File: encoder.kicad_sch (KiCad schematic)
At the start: 5 parts, among them IC1 AS5600-ASOT, J1 BM04B-SURS-TFLFSN, SW1 A6S-2104-H

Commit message: Reworked lots
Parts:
- removed SW1: A6S-2104-H, 2_POS_DIP:A6S-2104-H, symbol 2_POS_DIP:A6S-2104-H
- added H1, H2, H3: MountingHole, MountingHole:MountingHole_2.7mm_M2.5_ISO7380, symbol Mechanical:MountingHole
- added R1, R2: R, Resistor_SMD:R_0603_1608Metric_Pad0.98x0.95mm_HandSolder, symbol Device:R
- renumbered IC1 to U1
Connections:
- net +3.3V: now also R1.2
- net DIR: now also R1.1, R2.1
- net GND: now also J1.4 (SDA), R2.2; no longer J1.2 (GND)
- net SDA: now reaches U1.6 (SDA)
- net SDA: now also J1.2 (GND); no longer J1.4 (SDA)
- net SCL: now reaches J1.3 (SCL), U1.7 (SCL)
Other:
- moved on the sheet: J1

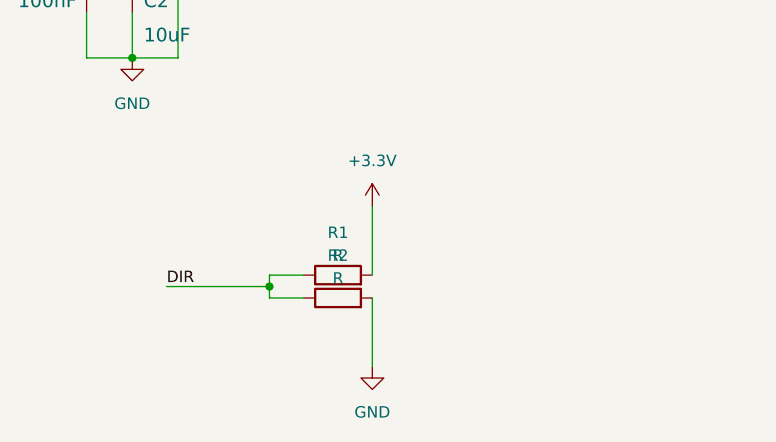
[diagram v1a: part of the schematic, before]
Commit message: schematic tweak
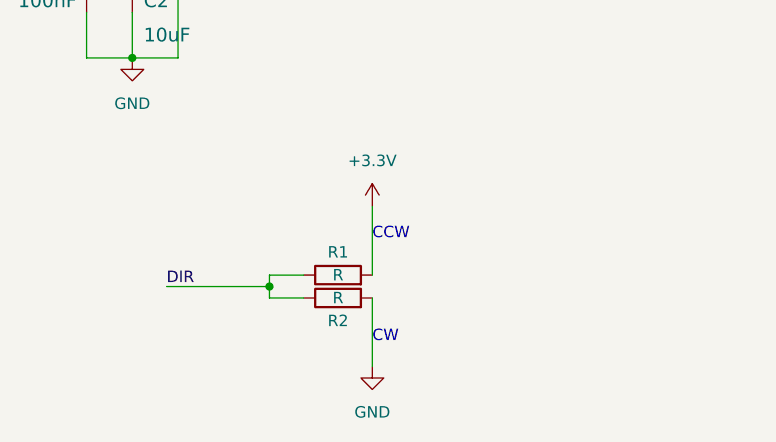
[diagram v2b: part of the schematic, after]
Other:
- note added: "CCW"
- note added: "CW"
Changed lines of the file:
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@@
     (stroke (width 0) (type default) (color 0 0 0 0))
+  )
+  (text "CW" (at 73.66 109.22 0)
+    (effects (font (size 1.27 1.27)) (justify left bottom))
+  )
+  (text "CCW" (at 73.66 97.79 0)
+    (effects (font (size 1.27 1.27)) (justify left bottom))
   )
   (label "SDA" (at 82.55 63.5 0)
@@
   )
   (symbol (lib_id "Device:R") (at 69.85 101.6 90) (unit 1)
-    (in_bom yes) (on_board yes) (fields_autoplaced)
-    (property "Reference" "R1" (id 0) (at 69.85 96.8842 90))
-    (property "Value" "R" (id 1) (at 69.85 99.4211 90))
+    (in_bom yes) (on_board yes)
+    (property "Reference" "R1" (id 0) (at 69.85 99.06 90))
+    (property "Value" "R" (id 1) (at 69.85 101.6 90))
     (property "Footprint" "Resistor_SMD:R_0603_1608Metric_Pad0.98x0.95mm_HandSolder" (id 2) (at 69.85 103.378 90)
       (effects (font (size 1.27 1.27)) hide)
@@
   )
   (symbol (lib_id "Device:R") (at 69.85 104.14 90) (unit 1)
-    (in_bom yes) (on_board yes) (fields_autoplaced)
-    (property "Reference" "R2" (id 0) (at 69.85 99.4242 90))
-    (property "Value" "R" (id 1) (at 69.85 101.9611 90))
+    (in_bom yes) (on_board yes)
+    (property "Reference" "R2" (id 0) (at 69.85 106.68 90))
+    (property "Value" "R" (id 1) (at 69.85 104.14 90))
     (property "Footprint" "Resistor_SMD:R_0603_1608Metric_Pad0.98x0.95mm_HandSolder" (id 2) (at 69.85 105.918 90)
       (effects (font (size 1.27 1.27)) hide)
